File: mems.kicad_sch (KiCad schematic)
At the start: 10 parts, among them U2 ICM-20602, U22 ICS-43434, U3 ICS-43434

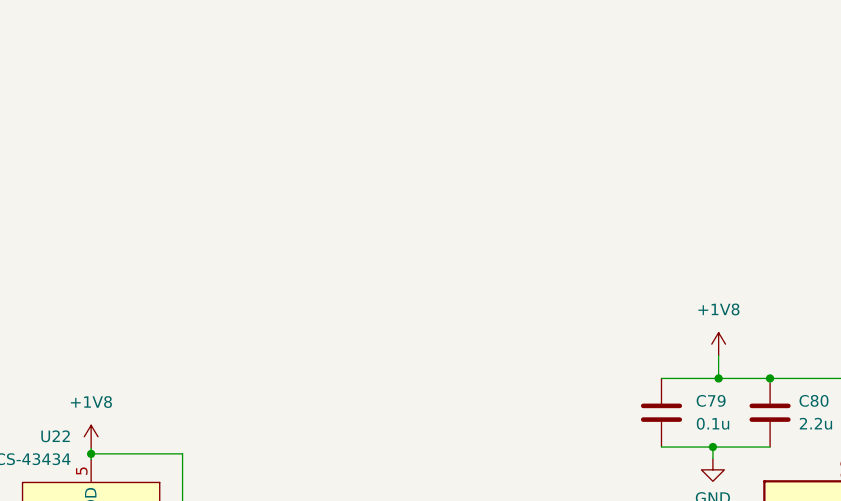
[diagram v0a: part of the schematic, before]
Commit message: Buzzer ajouté
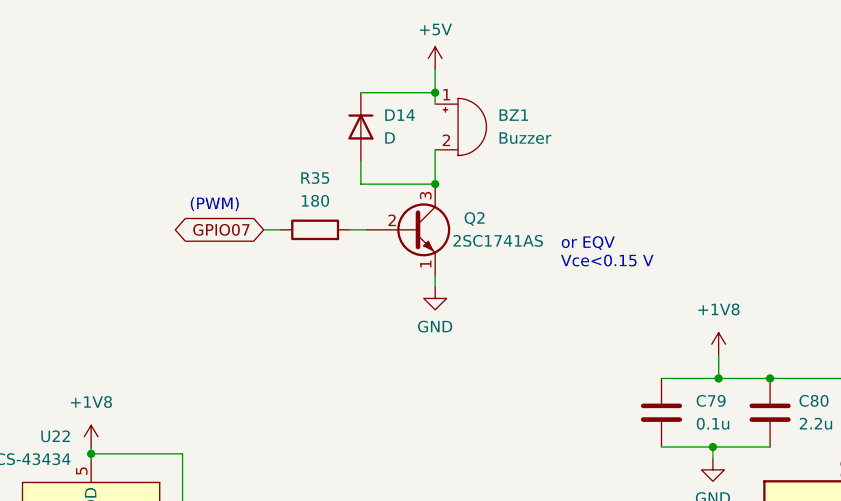
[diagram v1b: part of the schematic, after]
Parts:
- added BZ1: Buzzer, symbol Device:Buzzer
- added D14: D, symbol Device:D
- added Q2: 2SC1741AS, Package_TO_SOT_THT:TO-39-3, symbol Transistor_BJT:2N2219
- added R35: 180, symbol Device:R
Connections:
- net GND: now also Q2.1 (E)
- new net: Q2.2 (B), R35.2
- new net: BZ1.2 (+), D14.2 (A), Q2.3 (C)
- new net +5V: BZ1.1 (-), D14.1 (K)
- new net GPIO07: R35.1
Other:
- note added: "(PWM)"
- note added: "or EQV Vce<0.15 V"
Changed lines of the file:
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@@
   (junction (at 121.158 107.442) (diameter 0) (color 0 0 0 0)
   )
+  (junction (at 159.385 46.355) (diameter 0) (color 0 0 0 0)
+  )
   (junction (at 121.158 86.487) (diameter 0) (color 0 0 0 0)
   )
   (junction (at 71.628 97.282) (diameter 0) (color 0 0 0 0)
   )
+  (junction (at 159.385 56.515) (diameter 0) (color 0 0 0 0)
+  )
   (junction (at 81.788 107.442) (diameter 0) (color 0 0 0 0)
   )
@@
   )
   (no_connect (at 218.821 97.155))
+  (wire (pts (xy 151.13 46.355) (xy 159.385 46.355))
+    (stroke (width 0) (type default))
+  )
   (wire (pts (xy 220.726 109.855) (xy 220.726 113.665))
     (stroke (width 0) (type default))
   )
+  (wire (pts (xy 159.385 52.705) (xy 159.385 56.515))
+    (stroke (width 0) (type default))
+  )
   (wire (pts (xy 190.881 99.695) (xy 193.421 99.695))
     (stroke (width 0) (type default))
@@
     (stroke (width 0) (type default))
   )
+  (wire (pts (xy 159.385 43.815) (xy 159.385 46.355))
+    (stroke (width 0) (type default))
+  )
   (wire (pts (xy 221.996 81.915) (xy 220.726 81.915))
     (stroke (width 0) (type default))
@@
     (stroke (width 0) (type default))
   )
+  (wire (pts (xy 151.13 53.975) (xy 151.13 56.515))
+    (stroke (width 0) (type default))
+  )
   (wire (pts (xy 190.881 75.565) (xy 190.881 78.105))
     (stroke (width 0) (type default))
@@
     (stroke (width 0) (type default))
   )
+  (wire (pts (xy 159.385 66.675) (xy 159.385 67.945))
+    (stroke (width 0) (type default))
+  )
   (wire (pts (xy 81.788 85.852) (xy 81.788 86.487))
     (stroke (width 0) (type default))
@@
     (stroke (width 0) (type default))
   )
+  (wire (pts (xy 140.335 61.595) (xy 142.24 61.595))
+    (stroke (width 0) (type default))
+  )
   (wire (pts (xy 71.628 107.442) (xy 81.788 107.442))
     (stroke (width 0) (type default))
@@
     (stroke (width 0) (type default))
   )
+  (wire (pts (xy 149.86 61.595) (xy 151.765 61.595))
+    (stroke (width 0) (type default))
+  )
   (wire (pts (xy 101.473 99.822) (xy 105.283 99.822))
     (stroke (width 0) (type default))
   )
+  (wire (pts (xy 151.13 56.515) (xy 159.385 56.515))
+    (stroke (width 0) (type default))
+  )
   (wire (pts (xy 81.788 86.487) (xy 81.788 87.122))
     (stroke (width 0) (type default))
@@
     (stroke (width 0) (type default))
   )
+  (wire (pts (xy 159.385 46.355) (xy 159.385 47.625))
+    (stroke (width 0) (type default))
+  )
   (wire (pts (xy 208.661 81.915) (xy 208.661 86.995))
     (stroke (width 0) (type default))
@@
   (wire (pts (xy 121.158 107.442) (xy 121.158 108.712))
     (stroke (width 0) (type default))
+  )
+  (text "or EQV\nVce<0.15 V" (at 173.355 66.04 0)
+    (effects (font (size 1.27 1.27)) (justify left bottom))
+  )
+  (text "(PWM)\n" (at 132.08 59.69 0)
+    (effects (font (size 1.27 1.27)) (justify left bottom))
   )
   (global_label "MIC_SD" (shape output) (at 105.283 90.932 90) (fields_autoplaced)
@@
     )
   )
+  (global_label "GPIO07" (shape bidirectional) (at 140.335 61.595 180) (fields_autoplaced)
+    (effects (font (size 1.27 1.27)) (justify right))
+    (property "Intersheetrefs" "${INTERSHEET_REFS}" (at 129.3442 61.595 0)
+      (effects (font (size 1.27 1.27)) (justify right))
+    )
+  )
   (global_label "SPIO_MISO" (shape output) (at 190.881 97.155 180) (fields_autoplaced)
     (effects (font (size 1.27 1.27)) (justify right))
@@
     )
   )
+  (symbol (lib_id "Device:R") (at 146.05 61.595 90) (unit 1)
+    (in_bom yes) (on_board yes) (dnp no) (fields_autoplaced)
+    (property "Reference" "R35" (at 146.05 55.88 90)
+      (effects (font (size 1.27 1.27)))
+    )
+    (property "Value" "180" (at 146.05 58.42 90)
+      (effects (font (size 1.27 1.27)))
+    )
+    (property "Footprint" "" (at 146.05 63.373 90)
+      (effects (font (size 1.27 1.27)) hide)
+    )
+    (property "Datasheet" "~" (at 146.05 61.595 0)
+      (effects (font (size 1.27 1.27)) hide)
+    )
+    (pin "1")
+    (pin "2")
+    (instances
+      (project "jetson-orin-baseboard"
+        (path "/4b393452-b11e-416e-bc83-918ae3cab2f1/31739f71-b125-4faf-b93a-57120f7ec907"
+          (reference "R35") (unit 1)
+        )
+      )
+    )
+  )
   (symbol (lib_id "Device:C") (at 196.596 81.915 0) (unit 1)
     (in_bom yes) (on_board yes) (dnp no) (fields_autoplaced)
@@
         (path "/4b393452-b11e-416e-bc83-918ae3cab2f1/31739f71-b125-4faf-b93a-57120f7ec907"
           (reference "#PWR028") (unit 1)
+        )
+      )
+    )
+  )
+  (symbol (lib_id "power:+5V") (at 159.385 43.815 0) (unit 1)
+    (in_bom yes) (on_board yes) (dnp no) (fields_autoplaced)
+    (property "Reference" "#PWR074" (at 159.385 47.625 0)
+      (effects (font (size 1.27 1.27)) hide)
+    )
+    (property "Value" "+5V" (at 159.385 39.37 0)
+      (effects (font (size 1.27 1.27)))
+    )
+    (property "Footprint" "" (at 159.385 43.815 0)
+      (effects (font (size 1.27 1.27)) hide)
+    )
+    (property "Datasheet" "" (at 159.385 43.815 0)
+      (effects (font (size 1.27 1.27)) hide)
+    )
+    (pin "1")
+    (instances
+      (project "jetson-orin-baseboard"
+        (path "/4b393452-b11e-416e-bc83-918ae3cab2f1/31739f71-b125-4faf-b93a-57120f7ec907"
+          (reference "#PWR074") (unit 1)
         )
       )
@@
     )
   )
+  (symbol (lib_id "power:GND") (at 159.385 67.945 0) (unit 1)
+    (in_bom yes) (on_board yes) (dnp no) (fields_autoplaced)
+    (property "Reference" "#PWR077" (at 159.385 74.295 0)
+      (effects (font (size 1.27 1.27)) hide)
+    )
+    (property "Value" "GND" (at 159.385 72.39 0)
+      (effects (font (size 1.27 1.27)))
+    )
+    (property "Footprint" "" (at 159.385 67.945 0)
+      (effects (font (size 1.27 1.27)) hide)
+    )
+    (property "Datasheet" "" (at 159.385 67.945 0)
+      (effects (font (size 1.27 1.27)) hide)
+    )
+    (pin "1")
+    (instances
+      (project "jetson-orin-baseboard"
+        (path "/4b393452-b11e-416e-bc83-918ae3cab2f1/31739f71-b125-4faf-b93a-57120f7ec907"
+          (reference "#PWR077") (unit 1)
+        )
+      )
+    )
+  )
   (symbol (lib_id "I2S_MEMS_Microphone:ICS-43434") (at 81.788 97.282 0) (unit 1)
     (in_bom yes) (on_board yes) (dnp no) (fields_autoplaced)
@@
     )
   )
+  (symbol (lib_id "Transistor_BJT:2N2219") (at 156.845 61.595 0) (unit 1)
+    (in_bom yes) (on_board yes) (dnp no)
+    (property "Reference" "Q2" (at 162.56 60.325 0)
+      (effects (font (size 1.27 1.27)) (justify left))
+    )
+    (property "Value" " 2SC1741AS" (at 161.29 62.865 0)
+      (effects (font (size 1.27 1.27)) (justify left))
+    )
+    (property "Footprint" "Package_TO_SOT_THT:TO-39-3" (at 161.925 63.5 0)
+      (effects (font (size 1.27 1.27) italic) (justify left) hide)
+    )
+    (property "Datasheet" "http://www.onsemi.com/pub_link/Collateral/2N2219-D.PDF" (at 156.845 61.595 0)
+      (effects (font (size 1.27 1.27)) (justify left) hide)
+    )
+    (pin "1")
+    (pin "2")
+    (pin "3")
+    (instances
+      (project "jetson-orin-baseboard"
+        (path "/4b393452-b11e-416e-bc83-918ae3cab2f1/31739f71-b125-4faf-b93a-57120f7ec907"
+          (reference "Q2") (unit 1)
+        )
+      )
+    )
+  )
   (symbol (lib_id "Device:C") (at 131.318 103.632 0) (unit 1)
     (in_bom yes) (on_board yes) (dnp no) (fields_autoplaced)
@@
         (path "/4b393452-b11e-416e-bc83-918ae3cab2f1/31739f71-b125-4faf-b93a-57120f7ec907"
           (reference "#PWR026") (unit 1)
+        )
+      )
+    )
+  )
+  (symbol (lib_id "Device:D") (at 151.13 50.165 270) (unit 1)
+    (in_bom yes) (on_board yes) (dnp no) (fields_autoplaced)
+    (property "Reference" "D14" (at 153.67 48.895 90)
+      (effects (font (size 1.27 1.27)) (justify left))
+    )
+    (property "Value" "D" (at 153.67 51.435 90)
+      (effects (font (size 1.27 1.27)) (justify left))
+    )
+    (property "Footprint" "" (at 151.13 50.165 0)
+      (effects (font (size 1.27 1.27)) hide)
+    )
+    (property "Datasheet" "~" (at 151.13 50.165 0)
+      (effects (font (size 1.27 1.27)) hide)
+    )
+    (property "Sim.Device" "D" (at 151.13 50.165 0)
+      (effects (font (size 1.27 1.27)) hide)
+    )
+    (property "Sim.Pins" "1=K 2=A" (at 151.13 50.165 0)
+      (effects (font (size 1.27 1.27)) hide)
+    )
+    (pin "1")
+    (pin "2")
+    (instances
+      (project "jetson-orin-baseboard"
+        (path "/4b393452-b11e-416e-bc83-918ae3cab2f1/31739f71-b125-4faf-b93a-57120f7ec907"
+          (reference "D14") (unit 1)
         )
       )
@@
         )
       )
+    )
+  )
+  (symbol (lib_id "Device:Buzzer") (at 161.925 50.165 0) (unit 1)
+    (in_bom yes) (on_board yes) (dnp no) (fields_autoplaced)
+    (property "Reference" "BZ1" (at 166.37 48.895 0)
+      (effects (font (size 1.27 1.27)) (justify left))
+    )
+    (property "Value" "Buzzer" (at 166.37 51.435 0)
+      (effects (font (size 1.27 1.27)) (justify left))
+    )
+    (property "Footprint" "" (at 161.29 47.625 90)
+      (effects (font (size 1.27 1.27)) hide)
+    )
+    (property "Datasheet" "~" (at 161.29 47.625 90)
+      (effects (font (size 1.27 1.27)) hide)
+    )
+    (pin "1")
+    (pin "2")
+    (instances
+      (project "jetson-orin-baseboard"
+        (path "/4b393452-b11e-416e-bc83-918ae3cab2f1/31739f71-b125-4faf-b93a-57120f7ec907"
+          (reference "BZ1") (unit 1)
+        )
+      )

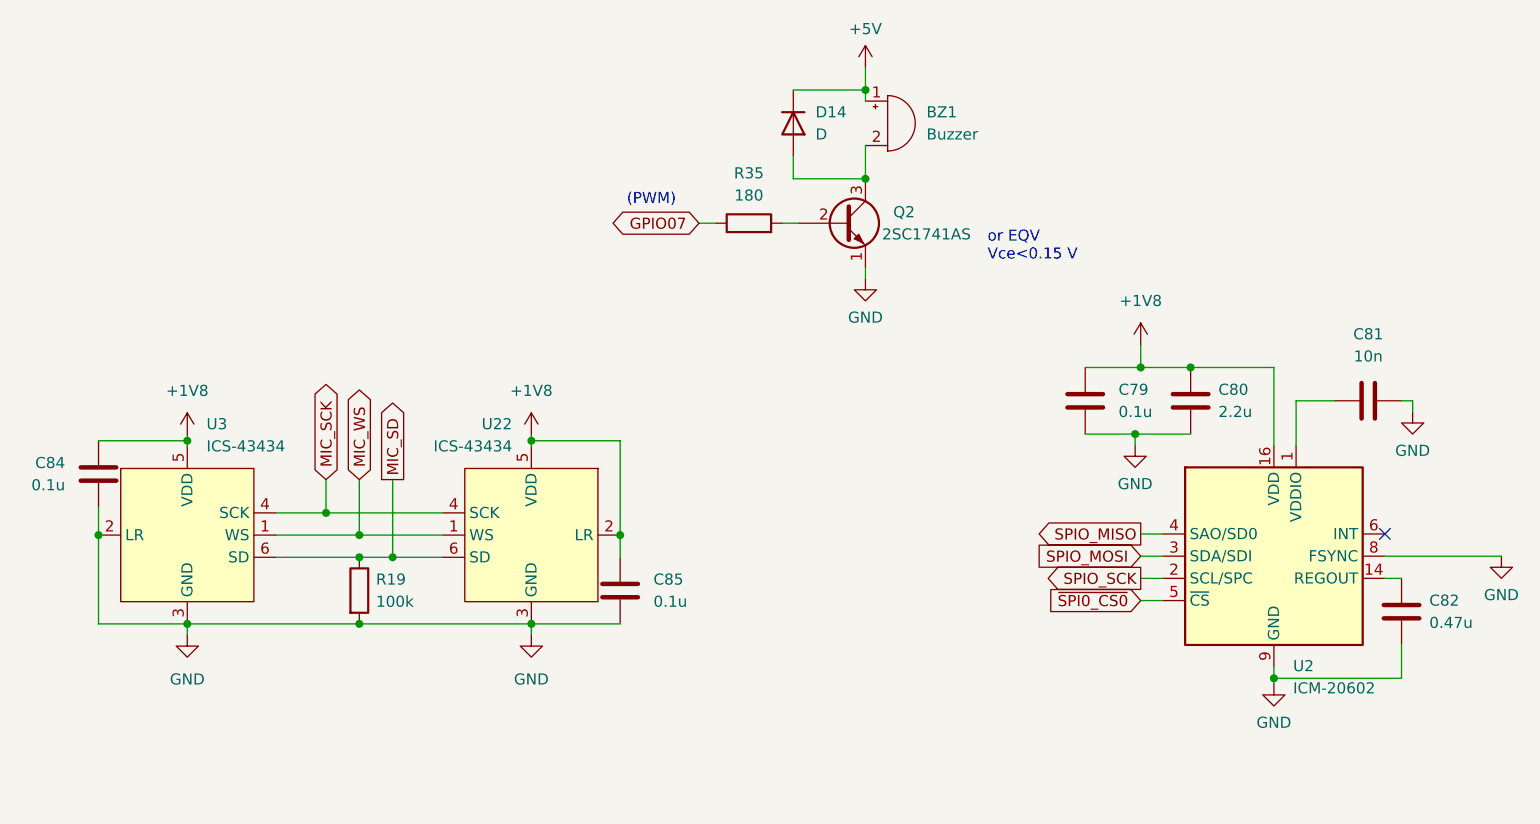
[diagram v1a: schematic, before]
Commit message: Schematic check
Include Pinmux and Schematic Check excels in doc folder and doing a lot of checking and correcting things.
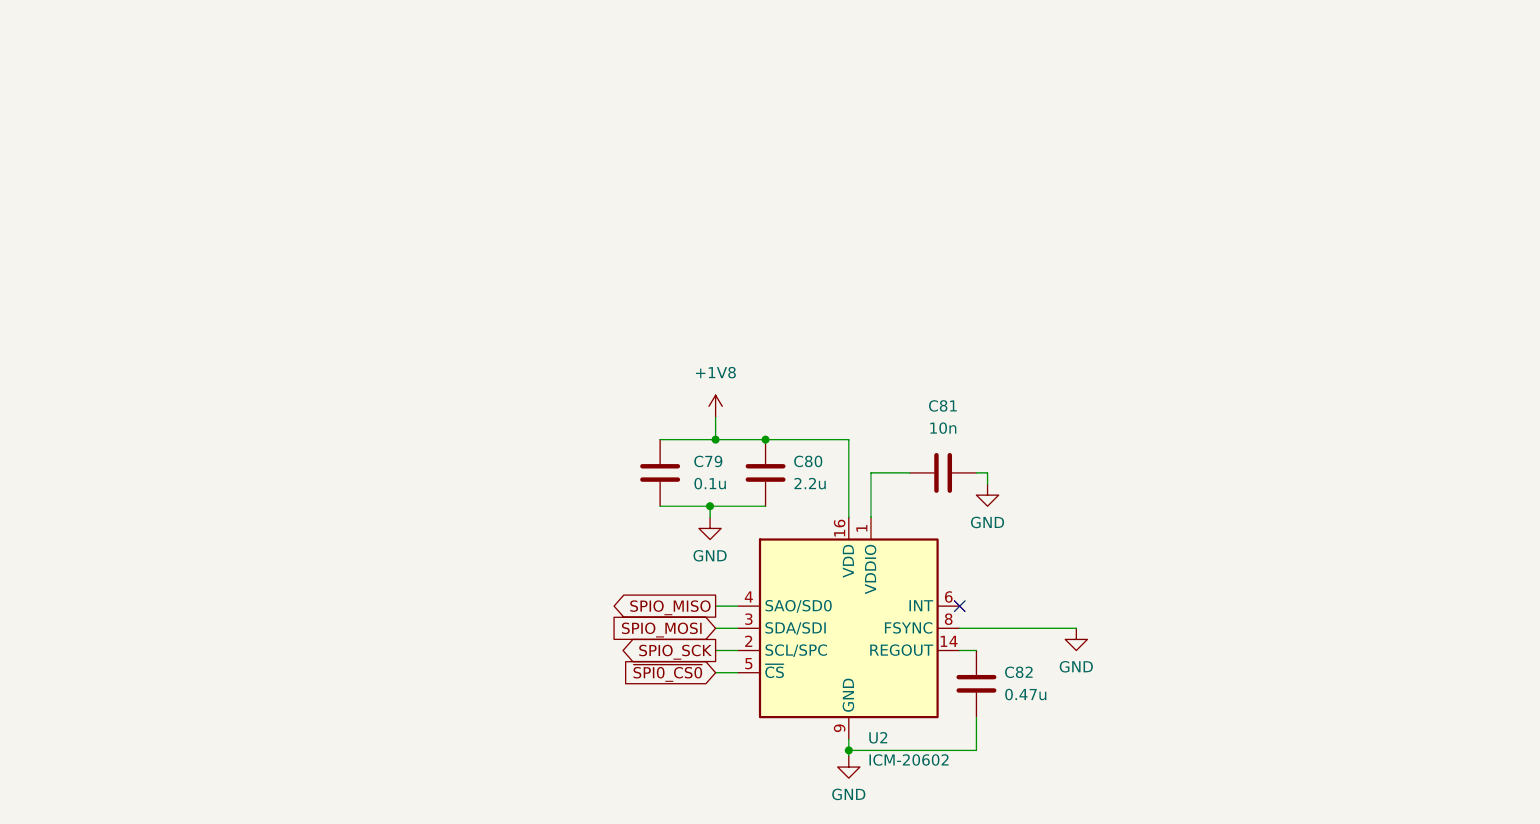
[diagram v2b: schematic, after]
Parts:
- removed BZ1: Buzzer, symbol Device:Buzzer
- removed C84, C85: 0.1u, symbol Device:C
- removed D14: D, symbol Device:D
- removed Q2: 2SC1741AS, Package_TO_SOT_THT:TO-39-3, symbol Transistor_BJT:2N2219
- removed R19: 100k, symbol Device:R
- removed R35: 180, symbol Device:R
- removed U22, U3: ICS-43434, symbol I2S_MEMS_Microphone:ICS-43434
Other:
- note removed: "(PWM)"
- note removed: "or EQV Vce<0.15 V"
- moved on the sheet: C79, C80, C81, C82, U2
